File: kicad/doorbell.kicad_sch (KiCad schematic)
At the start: 108 parts, among them J1 USB-JST, J2 WF26 bus, K1 GAQW212GS, K2 GAQY212GS, K3 GAQY412EH, K4 GAQY412EH, K5 G6K-2F-Y DC12, K6 GAQY412EH, Q3 AO3400A, Q4 AO3400A, SW1 BOOT, SW2 EN, SW3 Tueroeffner (door release), SW4 Sprechen/Hoeren (talk), U1 ESP32-S3-WROOM-1U-N16R8, U2 SGM2212-3.3, U3 ES8311, U4 LP5907MFX-3.3

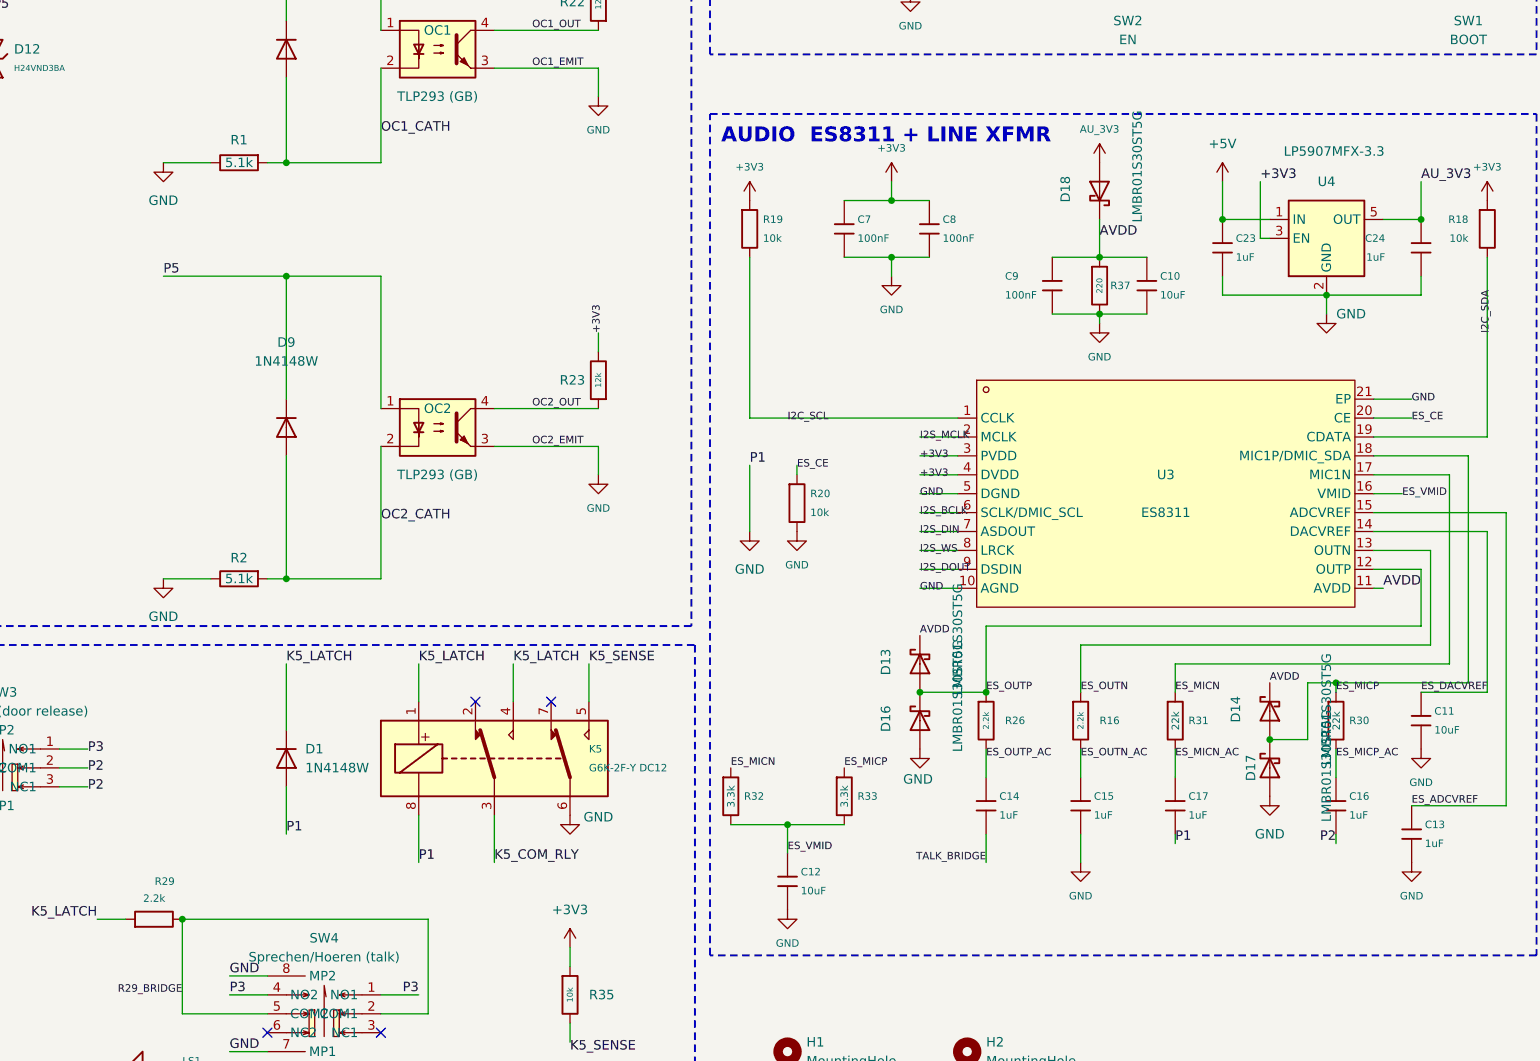
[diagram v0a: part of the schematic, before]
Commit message: hardware: close regulator stability margins
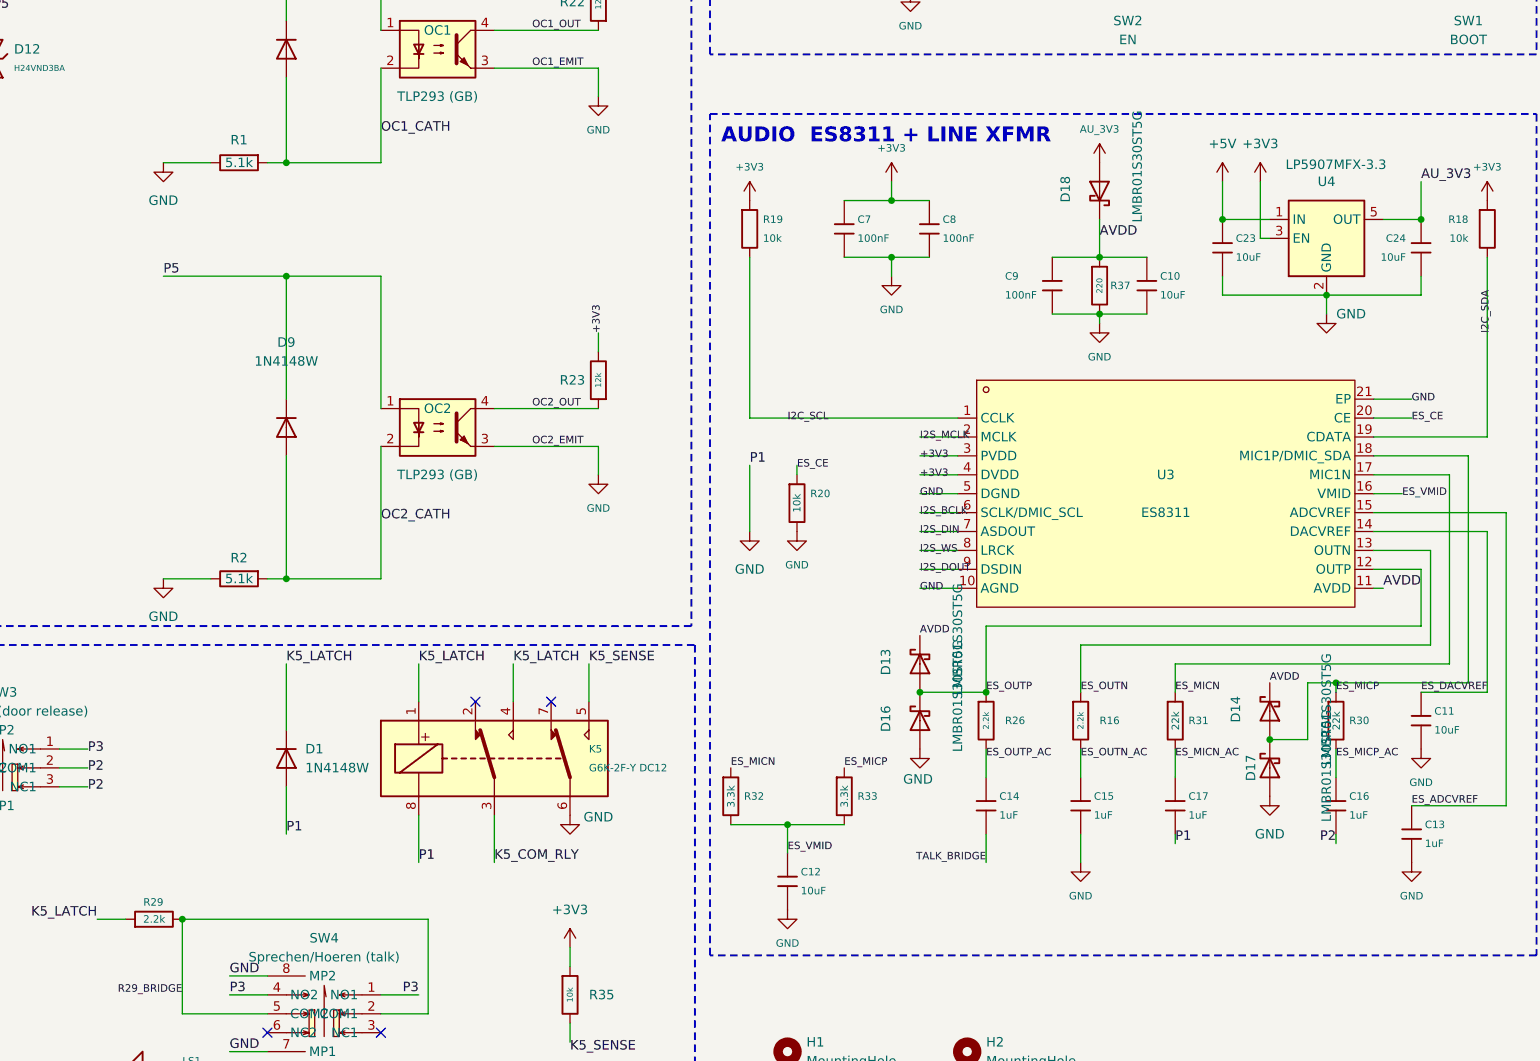
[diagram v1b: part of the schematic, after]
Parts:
- C23, C24: value 1uF -> 10uF; symbol PCM_JLCPCB-Capacitors:0603,1uF -> PCM_JLCPCB-Capacitors:0603,10uF; LCSC C15849 -> C19702; MPN CL10A105KB8NNNC -> CL10A106KP8NNNC

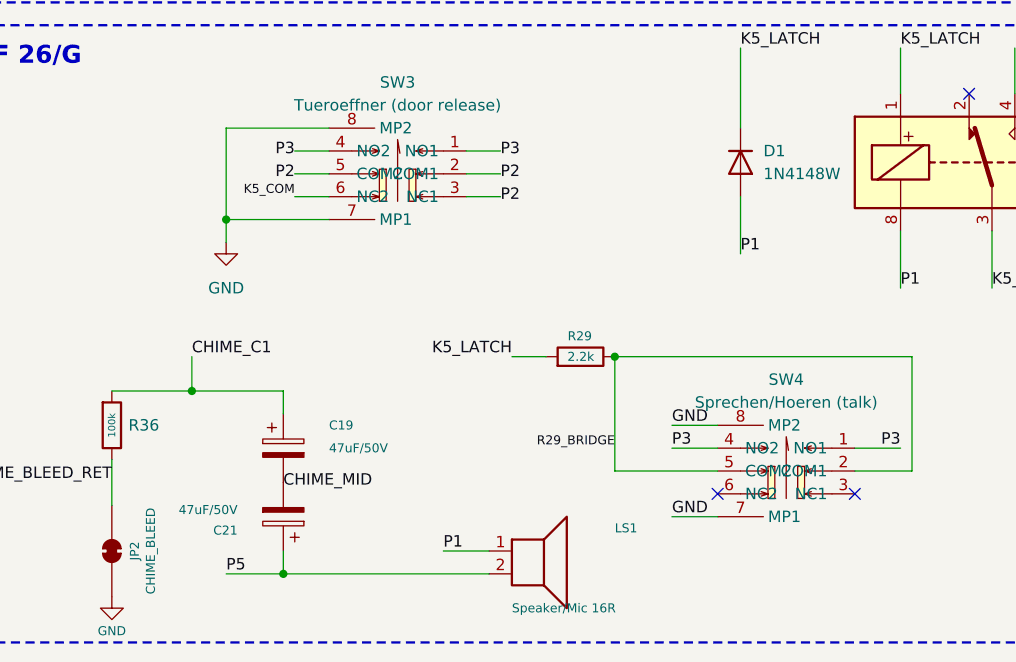
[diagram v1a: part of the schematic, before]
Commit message: Upgrade floor-call energy handling
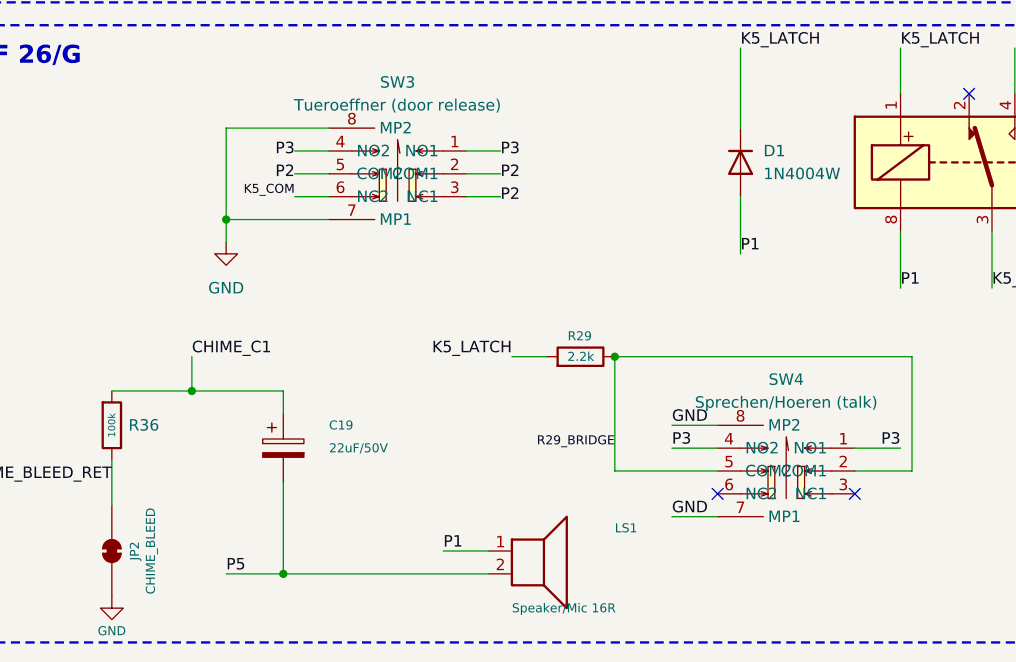
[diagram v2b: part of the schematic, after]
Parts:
- removed C21: 47uF/50V, rvt1h470m0607:CAP-SMD_BD6.3-L6.6-W6.6-LS7.6-FD, symbol Device:C_Polarized
- C19: value 47uF/50V -> 22uF/50V; footprint rvt1h470m0607:CAP-SMD_BD6.3-L6.6-W6.6-LS7.6-FD -> eeefk1h220p:CAP-SMD_BD6.3-L6.6-W6.6-FD; LCSC C3349 -> C128458; MPN RVT1H470M0607 -> EEEFK1H220P; Manufacturer Honor Elec -> Panasonic Industry
- D1: value 1N4148W -> 1N4004W; footprint Diode_SMD:D_SOD-123 -> 1n4004w:SOD-123FL_L2.7-W1.8-LS3.8-RD; symbol Diode:1N4148W -> 1n4004w:1N4004W_C18199087; LCSC C81598 -> C18199087; MPN (none) -> 1N4004W; Manufacturer (none) -> R+O
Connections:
- net CHIME_MID is gone; now on net P5: C19.2

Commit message: Derisk V4.2 hardware changes
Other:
- note added: "HOUSE BELL / Türruf (P1->P4)"
- note removed: "HOUSE BELL / Tuerruf (P1->P4)"

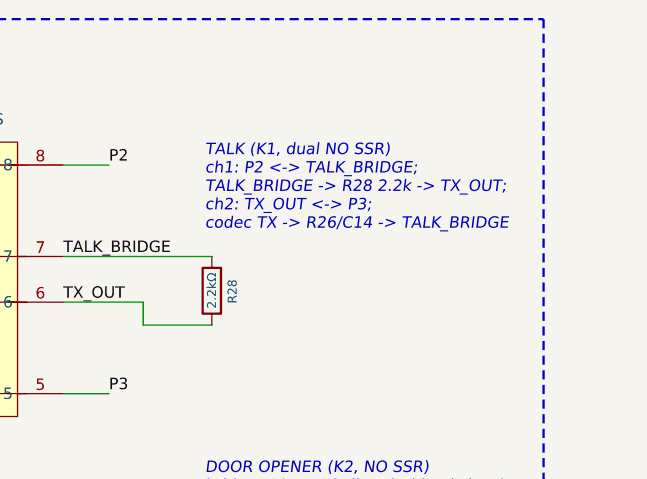
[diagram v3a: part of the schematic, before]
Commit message: Add TX bridge precharge network
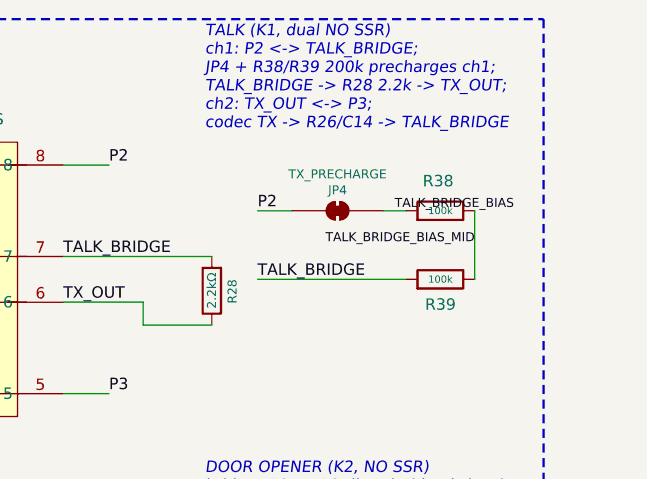
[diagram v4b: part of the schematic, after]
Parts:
- added JP4: TX_PRECHARGE, Jumper:SolderJumper-2_P1.3mm_Bridged_RoundedPad1.0x1.5mm, symbol Jumper:SolderJumper_2_Bridged
- added R38, R39: 100k, PCM_JLCPCB:R_0603, symbol PCM_JLCPCB-Resistors:0603,100kΩ
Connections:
- net P2: now also JP4.1 (A)
- net TALK_BRIDGE: now also R39.1
- new net TALK_BRIDGE_BIAS: JP4.2 (B), R38.1
- new net TALK_BRIDGE_BIAS_MID: R38.2, R39.2
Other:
- note added: "TALK (K1, dual NO SSR) ch1: P2 <-> TALK_BRIDGE; JP4 + R38/R39 200k precharges ch1; TALK_BRIDGE -> R28 2.2k -> TX_OUT; ch2: TX_OUT <-> P3; codec TX -> R26/C14 -> TALK_BRIDGE"
- note removed: "TALK (K1, dual NO SSR) ch1: P2 <-> TALK_BRIDGE; TALK_BRIDGE -> R28 2.2k -> TX_OUT; ch2: TX_OUT <-> P3; codec TX -> R26/C14 -> TALK_BRIDGE"

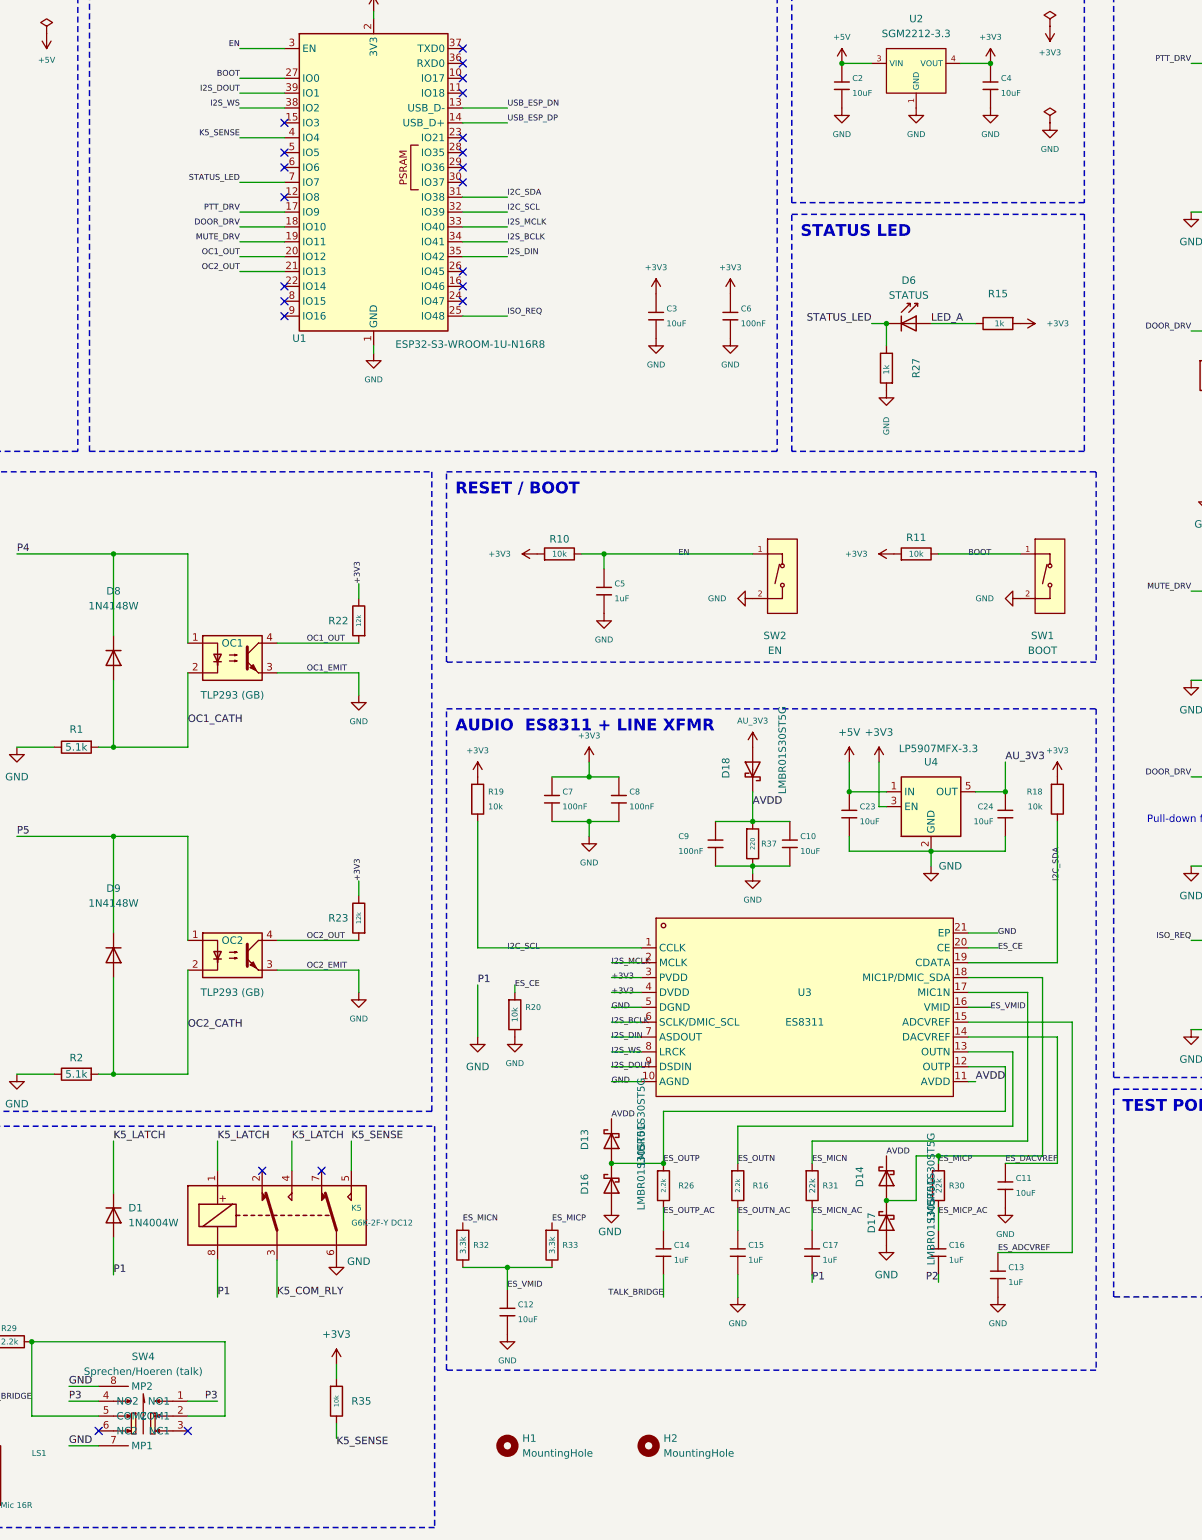
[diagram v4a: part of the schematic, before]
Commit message: Tidy KiCad schematic layout
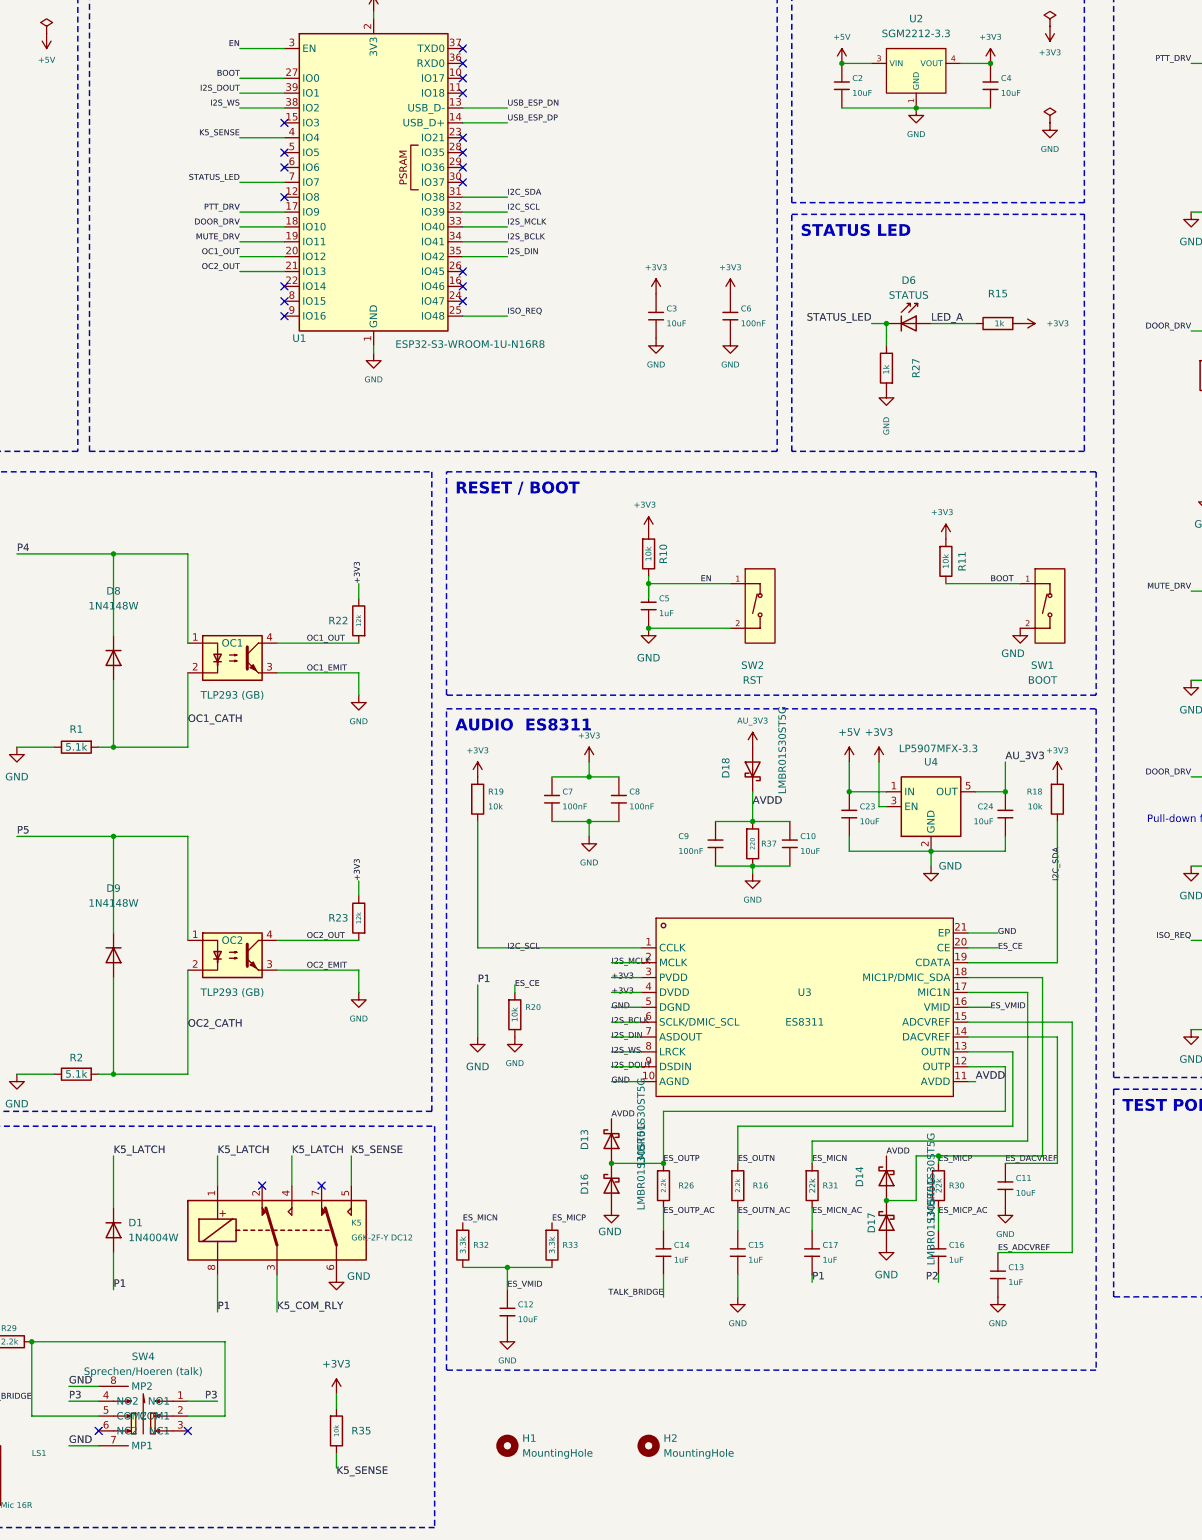
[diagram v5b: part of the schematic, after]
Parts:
- SW2: value EN -> RST
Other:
- note added: "AUDIO ES8311"
- note removed: "AUDIO ES8311 + LINE XFMR"
- moved on the sheet: C5, D1, K5, R10, R11, R35, SW1, SW2

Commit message: Rename internal nets for clarity
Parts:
- TP4: value AU_3V3 -> AVDD_PRE
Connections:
- net K5_COM_RLY is gone; now on net K5_COM: K4.3, K5.3
- net K5_COM: no longer K4.4, SW3.6 (NC2)
- net AU_3V3 renamed AVDD_PRE
- net CHIME_C1 renamed CHIME_POS
- net ISO_REQ renamed P4_ISO
- net K1_LED_A renamed K1A_A
- net K1_LED_B renamed K1B_A
- net K2_CATH renamed K2_K
- net K2_LED renamed K2_A
- net K3_LED renamed K3_A
- net K4_LED renamed K4_A
- net K5_SENSE renamed K5_SENSE_N
- net K6_LED renamed K6_A
- net OC1_CATH renamed OC1_K
- net OC1_OUT renamed P4_SENSE_N
- net OC2_CATH renamed OC2_K
- net OC2_OUT renamed P5_SENSE_N
- net R29_BRIDGE renamed TALK_SW
- net STATUS_LED renamed LED_K
- net TALK_BRIDGE_BIAS renamed PRECHG_IN
- net TALK_BRIDGE_BIAS_MID renamed PRECHG_MID
- new net SEAL_IN: K4.4, SW3.6 (NC2)
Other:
- note added: "CHIME SUPPRESS (K3, NC SSR) opens the C1 path (P4<->CHIME_POS); mutes gong; line 4 + latch intact"
- note removed: "CHIME SUPPRESS (K3, NC SSR) opens the C1 path (P4<->CHIME_C1); mutes gong; line 4 + latch intact"

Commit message: Renumber solder jumpers consecutively
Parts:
- renumbered JP2 to JP1, JP3 to JP2, JP4 to JP3

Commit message: Improve V4.2 commissioning coverage
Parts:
- added TP10: K5_LATCH, TestPoint:TestPoint_Pad_D1.5mm, symbol Connector:TestPoint
- added TP11: AVDD, TestPoint:TestPoint_Pad_D1.5mm, symbol Connector:TestPoint
- added TP9: TALK_BRIDGE, TestPoint:TestPoint_Pad_D1.5mm, symbol Connector:TestPoint
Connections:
- net AVDD: now also TP11.1
- net K5_LATCH: now also TP10.1
- net TALK_BRIDGE: now also TP9.1
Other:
- moved on the sheet: TP1, TP2, TP3, TP4, TP5, TP6, TP7, TP8
